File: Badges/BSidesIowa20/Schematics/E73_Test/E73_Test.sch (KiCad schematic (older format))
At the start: 27 parts, among them J1 Conn_01x02, J2 Oled, J4 Conn_02x04_Odd_Even, J7 USB_C_Receptacle, SW2 SW_DIP_x01, SW4 SW_DIP_x01, U2 TLV1117-33, U3 HX4056, U5 K1-5202UA-03(5Way_Switch)

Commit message: Putting stuff together
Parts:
- removed U5: K1-5202UA-03(5Way_Switch), Dragos:K1-5202UA-03(5way-switch), symbol dragos-rescue:K1-5202UA-03(5Way_Switch)-Dragos
- added L?: L_Small, symbol Device:L_Small
- added U?: BBQ10KBD, symbol Keyboard:BBQ10KBD
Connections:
- net VBUS is gone; now on net +5V: C14.2, U3.4 (Vin)
- net +3V3: no longer C3.2, U2.2 (VO)
- net +5V: no longer C2.2, U2.3 (VI)
- net VCC: now also C3.2, U2.2 (VO), U?.2 (MIC_VDD); no longer Power->1.2 (B)
- net VDD: now also C2.2, U2.3 (VI)
- net VDDA: now also Power->1.2 (B)
- net VSS: now also L?.2, U?.1 (GND), U?.11 (GND), U?.12 (GND), U?.13 (GND), U?.14 (GND), U?.15 (GND), U?.16 (GND), U?.28 (GND), U?.5 (GND)
- net IO27: no longer names the net of U3.6 (STAT2)
- new net: L?.1, U?.4 (AGND)
- new net COL1: U?.7 (COL1)
- new net COL2: U?.9 (COL2)
- new net COL3: U?.10 (COL3)
- new net COL4: U?.17 (COL4)
- new net COL5: U?.19 (COL5)
- new net LEDA1: U?.26 (LEDA_1_2)
- new net LEDA2: U?.24 (LEDA_3_4)
- new net LEDK1: U?.25 (LEDK_1_4)
- new net LEDK2: U?.23 (LEDK_2_3)
- new net MIC: U?.3 (MIC)
- new net ROW1: U?.6 (ROW1)
- new net ROW2: U?.8 (ROW2)
- new net ROW3: U?.18 (ROW3)
- new net ROW4: U?.20 (ROW4)
- new net ROW5: U?.21 (ROW5)
- new net ROW6: U?.22 (ROW6)
- new net ROW7: U?.27 (ROW7)
- no-connect marks 11 -> 12
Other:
- moved on the sheet: BT1, C14, C17, C2, C3, J2, J4, Power->1, R2, R5, SW2, U2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

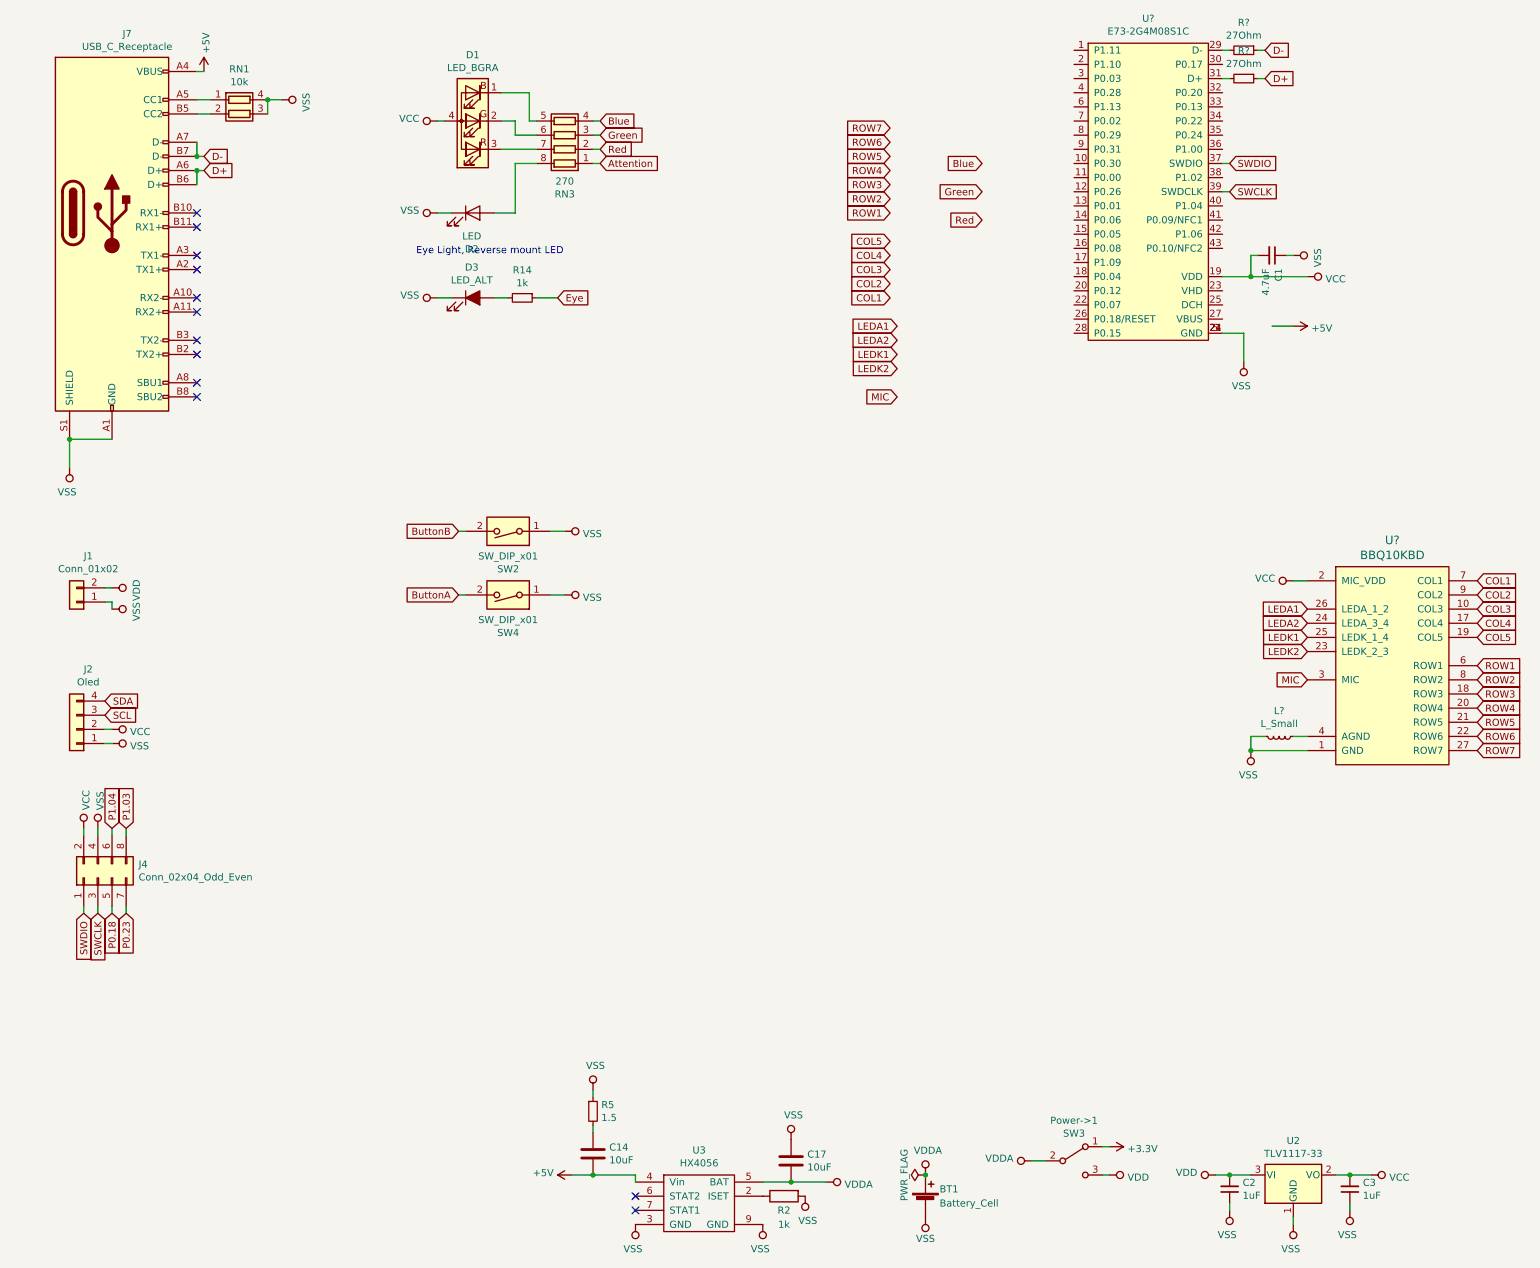
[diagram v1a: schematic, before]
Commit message: FJE Badge Charlieplexing done
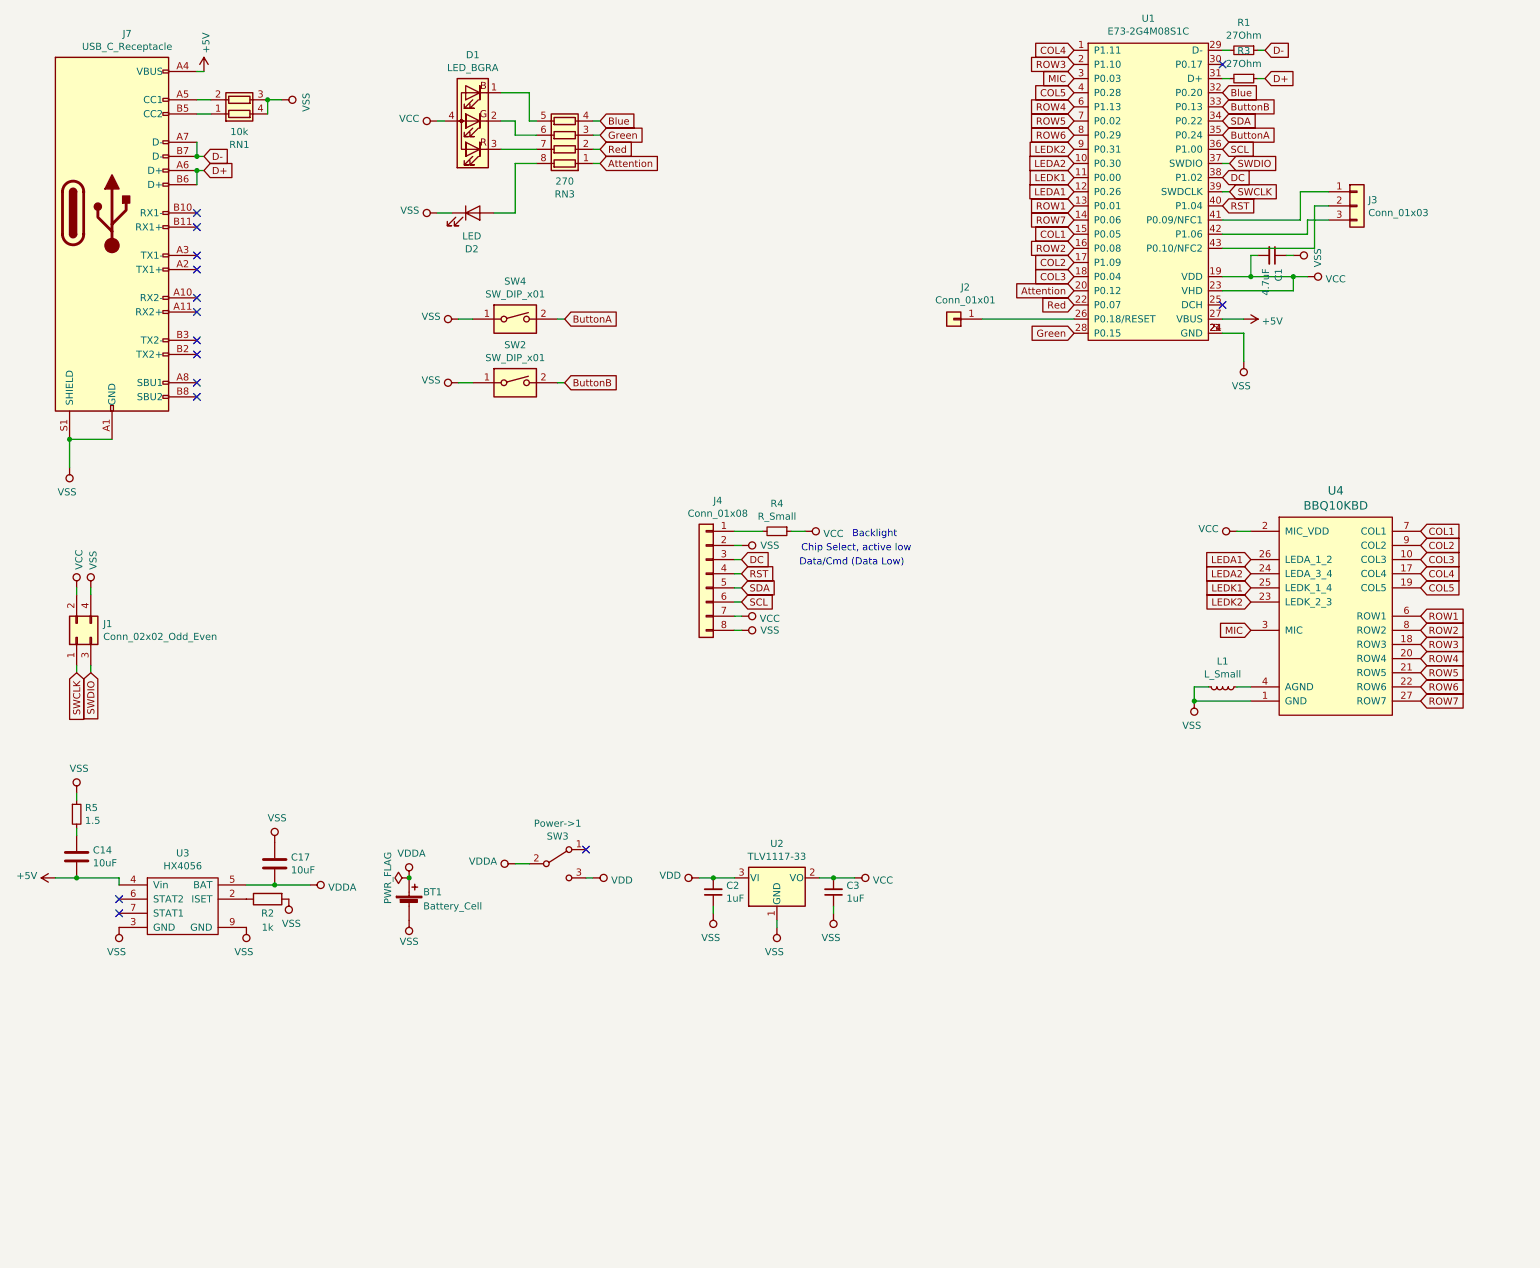
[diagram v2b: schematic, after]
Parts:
- removed D3: LED_ALT, Dragos:T776-ReverseMountLED, symbol Device:LED_ALT
- removed J1: Conn_01x02, symbol dragos-rescue:Conn_01x02-badge-rescue
- removed J2: Oled, Dragos:Oled, symbol dragos-rescue:Conn_01x04-badge-rescue
- removed J4: Conn_02x04_Odd_Even, Connector_PinHeader_2.54mm:PinHeader_2x04_P2.54mm_Vertical, symbol Connector_Generic:Conn_02x04_Odd_Even
- removed R14: 1k, Resistor_SMD:R_0805_2012Metric, symbol Device:R_Small
- added J1: Conn_02x02_Odd_Even, Connector_PinHeader_2.54mm:PinHeader_2x02_P2.54mm_Vertical, symbol Connector_Generic:Conn_02x02_Odd_Even
- added J2: Conn_01x01, Connector_PinHeader_2.54mm:PinHeader_1x01_P2.54mm_Vertical, symbol badge-rescue:Conn_01x01
- added J3: Conn_01x03, Connector_PinHeader_2.54mm:PinHeader_1x03_P2.54mm_Vertical, symbol Connector_Generic:Conn_01x03
- added J4: Conn_01x08, Connector_PinHeader_2.54mm:PinHeader_1x08_P2.54mm_Vertical, symbol Connector_Generic:Conn_01x08
- added R4: R_Small, Resistor_SMD:R_0805_2012Metric, symbol Device:R_Small
- BT1: footprint Battery_Holders:Keystone_3009_1x2450-CoinCell -> Tests:Dongguan14500
- C14, C17: footprint Capacitors_SMD:C_0805_HandSoldering -> Capacitor_SMD:C_0805_2012Metric
- L1: renamed from L?; footprint (none) -> Inductor_SMD:L_0805_2012Metric
- R1, R3: renamed from R?; footprint (none) -> Resistor_SMD:R_0805_2012Metric
- R2: footprint Resistors_SMD:R_0805_HandSoldering -> Resistor_SMD:R_0805_2012Metric
- R5: footprint Resistors_SMD:R_0805 -> Resistor_SMD:R_0805_2012Metric
- U1: renamed from U?; footprint (none) -> E73:E73-2G4M08S1C
- U3: footprint Badge:HX4056 -> Package_SO:HSOP-8-1EP_3.9x4.9mm_P1.27mm_EP2.41x3.1mm
- U4: renamed from U?; footprint (none) -> Connectors_Hirose_extra:BM14B(0.8)-24DS-0.4V(53)
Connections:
- net +5V: now also U1.27 (VBUS)
- net Attention: now also U1.20 (P0.12)
- net Blue: now also U1.32 (P0.20)
- net ButtonA: now also U1.35 (P0.24)
- net ButtonB: now also U1.33 (P0.13)
- net COL1: now also U1.15 (P0.05)
- net COL2: now also U1.17 (P1.09)
- net COL3: now also U1.18 (P0.04)
- net COL4: now also U1.1 (P1.11)
- net COL5: now also U1.4 (P0.28)
- net Green: now also U1.28 (P0.15)
- net LEDA1: now also U1.12 (P0.26)
- net LEDA2: now also U1.10 (P0.30)
- net LEDK1: now also U1.11 (P0.00)
- net LEDK2: now also U1.9 (P0.31)
- net MIC: now also U1.3 (P0.03)
- net ROW1: now also U1.13 (P0.01)
- net ROW2: now also U1.16 (P0.08)
- net ROW3: now also U1.2 (P1.10)
- net ROW4: now also U1.6 (P1.13)
- net ROW5: now also U1.7 (P0.02)
- net ROW6: now also U1.8 (P0.29)
- net ROW7: now also U1.14 (P0.06)
- net Red: now also U1.22 (P0.07)
- net SCL: now also U1.36 (P1.00), J4.6 (Pin_6)
- net SDA: now also U1.34 (P0.22), J4.5 (Pin_5)
- net SWCLK: now also J1.1 (Pin_1)
- net SWDIO: now also J1.3 (Pin_3)
- net VCC: now also U1.23 (VHD), J1.2 (Pin_2), J4.7 (Pin_7), R4.1
- net VSS: now also J1.4 (Pin_4), J4.2 (Pin_2), J4.8 (Pin_8)
- net at J7.A5 (CC1): now also RN1.2 (R2.1); no longer RN1.1 (R1.1)
- net at J7.B5 (CC2): now also RN1.1 (R1.1); no longer RN1.2 (R2.1)
- net at U1.26 (P0.18/RESET): now also J2.1 (Pin_1)
- net DC: now reaches U1.38 (P1.02)
- net DC: now also J4.3 (Pin_3)
- net RST: now reaches U1.40 (P1.04)
- net RST: now also J4.4 (Pin_4)
- net at U1.41 (P0.09/NFC1): now also J3.1 (Pin_1)
- net at U1.42 (P1.06): now also J3.3 (Pin_3)
- net at U1.43 (P0.10/NFC2): now also J3.2 (Pin_2)
- net +3V3: no longer names the net of Power->1.1 (A)
- new net: J4.1 (Pin_1), R4.2
- no-connect marks 12 -> 15
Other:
- note added: "Backlight"
- note added: "Chip Select, active low"
- note added: "Data/Cmd (Data Low)\n"
- note removed: "Eye Light, Reverse mount LED"
- moved on the sheet: BT1, C14, C17, C2, C3, L1, Power->1, R2, R5, SW2, SW4, U2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
